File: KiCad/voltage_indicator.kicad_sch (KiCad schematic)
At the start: 52 parts, among them Q4 BC857C, U34 LT6700-1, U35 VIPER012BHSTR, U36 PEME1-S24-S5-S

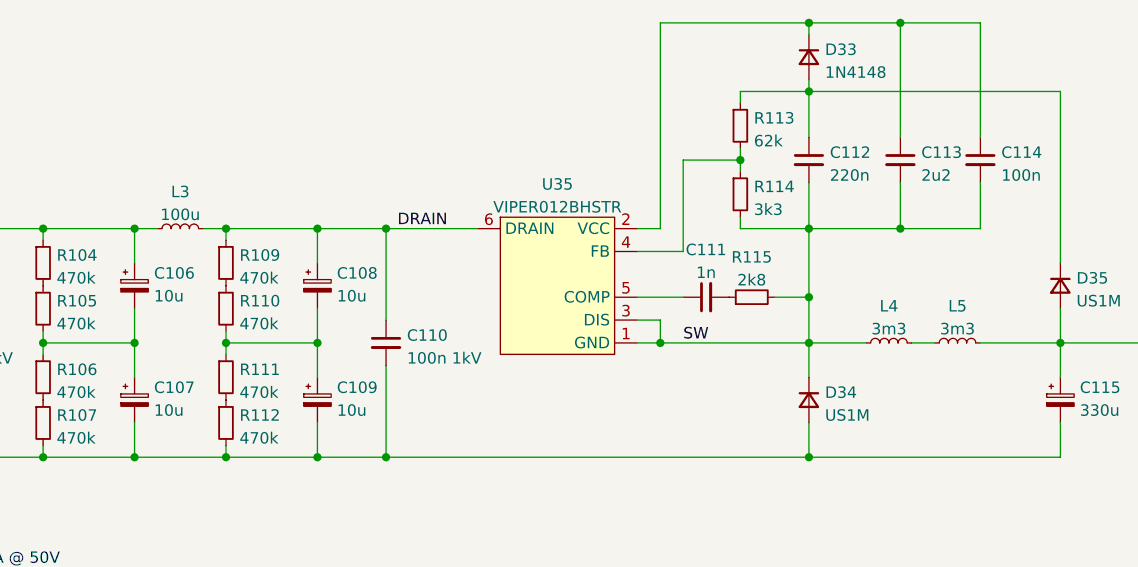
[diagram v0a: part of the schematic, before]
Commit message: Port to Kicad 7, small changes in auto-reset feature
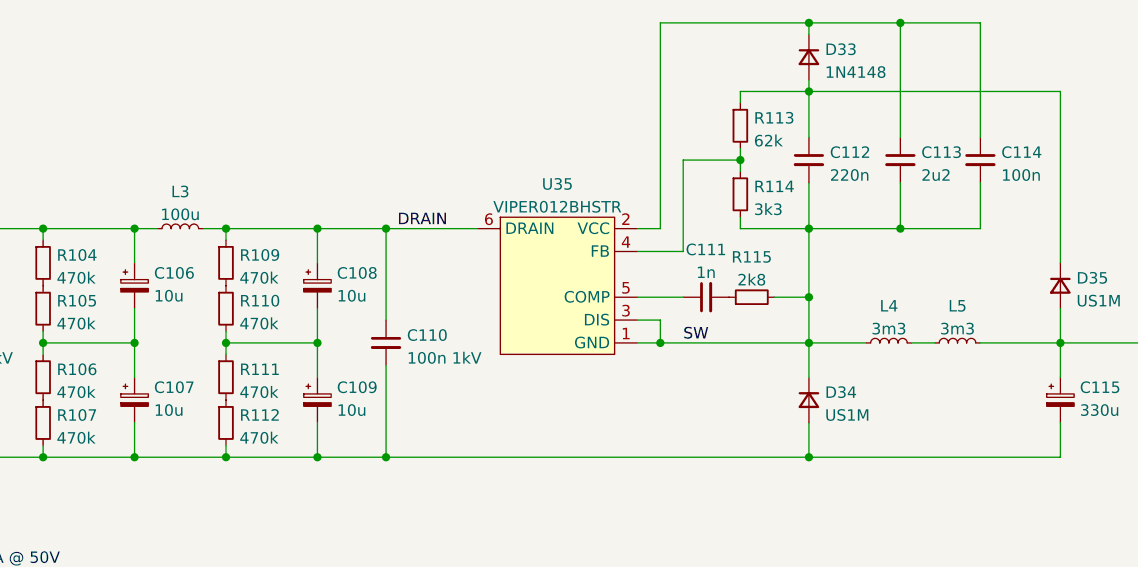
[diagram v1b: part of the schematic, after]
